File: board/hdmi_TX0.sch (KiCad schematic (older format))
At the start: 26 parts

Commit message: Updating from template.
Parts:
- removed CTX009: 0.33uF, Capacitors_SMD:C_0603, symbol C
- removed CTX010, CTX011: 0.1uF, Capacitors_SMD:C_0603, symbol C
- removed RTX006: 100K, Resistors_SMD:R_0402, symbol R
- removed UTX001: ΜA78L00, ma78l00:μA78L00, symbol ΜA78L00
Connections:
- net labels removed: VCC12V0
- wire segments 122 -> 125
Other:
- note added: "This sheet is generated from ../external/templates/\nDO NOT MODIFY!!!\n7e53b7f"
- note removed: "This sheet is generated from ../external/templates/\nDO NOT MODIFY!!!\nc4498e4"
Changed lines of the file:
@@
 LIBS:contrib
 LIBS:valves
-LIBS:pmod
+LIBS:pmod-conn_6x2
+LIBS:ma78l00
 LIBS:hdmi
 LIBS:ptn3363
-LIBS:ma78l00
-LIBS:pmod-conn_6x2
-LIBS:EEPROM
-LIBS:xc9140
-LIBS:hdmi-expansion-module-cache
+LIBS:hdmi_TXn-cache
 EELAYER 25 0
 EELAYER END
 $Descr A3 16535 11693
 encoding utf-8
-Sheet 2 2
+Sheet 1 1
 Title ""
 Date ""
@@
 F 0 "DTX001" H 10600 5540 50  0000 C CNN
 F 1 "D" H 10600 5340 50  0000 C CNN
-F 2 "Diodes_SMD:SOD-523" H 10600 5440 50  0000 C CNN
+F 2 "Diodes_SMD:SOD-523" H 10600 5440 50  0001 C CNN
 F 3 "" H 10600 5440 50  0000 C CNN
 F 4 "BAS16XV2T1G" H 10600 5440 60  0001 C CNN "manf#"
@@
 AR Path="/57C07751" Ref="RTX008"  Part="1"
 AR Path="/57C01383/57C07751" Ref="RTX003"  Part="1"
-AR Path="/5802F547/57C07751" Ref="RTX008"  Part="1"
 F 0 "RTX008" V 10700 4950 50  0000 C CNN
 F 1 "27K" V 10607 4951 50  0000 C CNN
@@
 AR Path="/57C07753" Ref="RTX002"  Part="1"
 AR Path="/57C01383/57C07753" Ref="RTX001"  Part="1"
-AR Path="/5802F547/57C07753" Ref="RTX002"  Part="1"
 F 0 "RTX002" V 3800 4400 50  0000 C CNN
 F 1 "2k2" V 3907 4401 50  0000 C CNN
@@
 AR Path="/57C07755" Ref="RTX001"  Part="1"
 AR Path="/57C01383/57C07755" Ref="RTX002"  Part="1"
-AR Path="/5802F547/57C07755" Ref="RTX001"  Part="1"
 F 0 "RTX001" V 4080 4400 50  0000 C CNN
 F 1 "2k2" V 4007 4401 50  0000 C CNN
@@
 	11750 4850 11600 4850
 Wire Wire Line
-	11600 4850 11600 6900
+	11600 4850 11600 5150
+Wire Wire Line
+	11600 5150 11600 5450
+Wire Wire Line
+	11600 5450 11600 5750
+Wire Wire Line
+	11600 5750 11600 6350
+Wire Wire Line
+	11600 6350 11600 6900
 Wire Wire Line
 	11750 5150 11600 5150
@@
 	6400 5800 6750 5800
 Wire Wire Line
-	8150 6600 9000 6600
+	8150 6600 8550 6600
+Wire Wire Line
+	8550 6600 9000 6600
 Wire Wire Line
 	8150 6400 9000 6400
 Wire Wire Line
-	7400 3750 7500 3750
-Wire Wire Line
-	7450 3750 7450 3600
+	7400 3750 7450 3750
+Wire Wire Line
+	7450 3750 7500 3750
+Wire Wire Line
+	7450 3200 7450 3750
 Connection ~ 7450 3750
 Wire Wire Line
@@
 Connection ~ 11600 6350
 Wire Wire Line
-	9800 5950 11750 5950
+	9800 5950 10600 5950
+Wire Wire Line
+	10600 5950 11750 5950
 Wire Wire Line
 	10600 5950 10600 5590
@@
 	4000 4100 4000 4250
 Wire Wire Line
-	3900 4100 4000 4100
+	3900 4100 3950 4100
+Wire Wire Line
+	3950 4100 4000 4100
 Text Label 3800 5900 2    60   ~ 0
 HDMIP_TX0_SCL
@@
 AR Path="/57C07769" Ref="RTX004"  Part="1"
 AR Path="/57C01383/57C07769" Ref="RTX004"  Part="1"
-AR Path="/5802F547/57C07769" Ref="RTX004"  Part="1"
 F 0 "RTX004" V 3800 5600 50  0000 C CNN
 F 1 "2k2" V 3907 5601 50  0000 C CNN
@@
 AR Path="/57B7FCE7" Ref="RTX005"  Part="1"
 AR Path="/57C01383/57B7FCE7" Ref="RTX005"  Part="1"
-AR Path="/5802F547/57B7FCE7" Ref="RTX005"  Part="1"
 F 0 "RTX005" V 4080 5600 50  0000 C CNN
 F 1 "2k2" V 4007 5601 50  0000 C CNN
@@
 AR Path="/57C0776D" Ref="RTX003"  Part="1"
 AR Path="/57C01383/57C0776D" Ref="RTX006"  Part="1"
-AR Path="/5802F547/57C0776D" Ref="RTX003"  Part="1"
 F 0 "RTX003" V 6580 6900 50  0000 C CNN
 F 1 "12k4" V 6507 6901 50  0000 C CNN
@@
 	3900 5300 3900 5450
 Wire Wire Line
-	3900 5300 4000 5300
+	3900 5300 3950 5300
+Wire Wire Line
+	3950 5300 4000 5300
 Wire Wire Line
 	4000 5300 4000 5450
@@
 AR Path="/57C07777" Ref="CTX017"  Part="1"
 AR Path="/57C01383/57C07777" Ref="CTX002"  Part="1"
-AR Path="/5802F547/57C07777" Ref="CTX017"  Part="1"
 F 0 "CTX017" H 8300 3750 30  0000 L CNN
 F 1 "100n" H 8300 3850 30  0000 L CNN
@@
 AR Path="/57C07779" Ref="CTX016"  Part="1"
 AR Path="/57C01383/57C07779" Ref="CTX001"  Part="1"
-AR Path="/5802F547/57C07779" Ref="CTX016"  Part="1"
 F 0 "CTX016" H 8350 3750 30  0000 L CNN
 F 1 "100n" H 8400 3850 30  0000 L CNN
@@
 $EndComp
 Wire Wire Line
-	8300 3600 8500 3600
+	8300 3600 8400 3600
+Wire Wire Line
+	8400 3600 8500 3600
 Wire Wire Line
 	8300 3600 8300 3700
@@
 	8300 4000 8300 4100
 Wire Wire Line
-	8300 4100 8500 4100
+	8300 4100 8400 4100
+Wire Wire Line
+	8400 4100 8500 4100
 Wire Wire Line
 	8500 4100 8500 4000
@@
 Text Label 9000 6400 2    60   ~ 0
 HDMI_TX0_HIZ_EN
-Text Label 1885 6870 0    60   ~ 0
+Text Label 4685 6670 2    60   ~ 0
 HDMI_TX0_HPD
+Text Label 4685 6570 2    60   ~ 0
+HDMI_TX0_SCL
 Text Label 1885 6670 0    60   ~ 0
-HDMI_TX0_SCL
-Text Label 1885 6770 0    60   ~ 0
 HDMI_TX0_SDA
 $Comp
@@
 	6500 7050 6500 7150
 Text Notes 670  10960 0    197  ~ 39
-This sheet is generated from ../external/templates/\nDO NOT MODIFY!!!\nc4498e4
-Wire Wire Line
-	2255 6970 2865 6970
-Wire Wire Line
-	2725 7070 2865 7070
+This sheet is generated from ../external/templates/\nDO NOT MODIFY!!!\n7e53b7f
+Wire Wire Line
+	2255 6970 2325 6970
+Wire Wire Line
+	2325 6970 2865 6970
+Wire Wire Line
+	2725 7070 2770 7070
+Wire Wire Line
+	2770 7070 2865 7070
 Wire Wire Line
 	2865 6570 1885 6570
@@
 	3755 6970 3665 6970
 Connection ~ 2325 6970
-Text Label 4685 6865 2    60   ~ 0
+Text Label 4685 6870 2    60   ~ 0
 HDMI_TX0_DDET
-Text Label 4685 6665 2    60   ~ 0
+Text Label 1885 6770 0    60   ~ 0
 HDMI_TX0_EQ1
-Text Label 4685 6765 2    60   ~ 0
+Text Label 1885 6870 0    60   ~ 0
 HDMI_TX0_DDC_EN
 Wire Wire Line
-	4685 6865 3665 6870
-Wire Wire Line
-	4685 6765 3665 6770
-Wire Wire Line
-	4685 6665 3665 6670
-Wire Wire Line
-	4685 6565 3665 6570
-Text Label 4685 6565 2    60   ~ 0
+	4685 6870 3665 6870
+Wire Wire Line
+	4685 6770 3665 6770
+Wire Wire Line
+	4685 6670 3665 6670
+Wire Wire Line
+	4685 6570 3665 6570
+Text Label 4685 6770 2    60   ~ 0
 HDMI_TX0_EQ0
 $Comp
@@
 	0    1    1    0
 $EndComp
-$Comp
-L ΜA78L00 UTX001
-U 1 1 57E8C5A1
-P 11700 8100
-F 0 "UTX001" H 12000 7800 60  0000 C CNN
-F 1 "ΜA78L00" H 11550 8350 60  0000 C CNN
-F 2 "ma78l00:μA78L00" H 11700 8100 60  0001 C CNN
-F 3 "" H 11700 8100 60  0000 C CNN
-F 4 "UA78L05ACPK" H 11700 8100 60  0001 C CNN "manf#"
-F 5 "296-11118-1-ND" H 11700 8100 60  0001 C CNN "digikey#"
-	1    11700 8100
-	1    0    0    -1
-$EndComp
-$Comp
-L C CTX009
-U 1 1 57E8C7B4
-P 10700 8400
-F 0 "CTX009" H 10725 8500 50  0000 L CNN
-F 1 "0.33uF" H 10725 8300 50  0000 L CNN
-F 2 "Capacitors_SMD:C_0603" H 10738 8250 50  0001 C CNN
-F 3 "" H 10700 8400 50  0000 C CNN
-	1    10700 8400
-	1    0    0    -1
-$EndComp
-$Comp
-L C CTX010
-U 1 1 57E8C84C
-P 12450 8400
-F 0 "CTX010" H 12475 8500 50  0000 L CNN
-F 1 "0.1uF" H 12475 8300 50  0000 L CNN
-F 2 "Capacitors_SMD:C_0603" H 12488 8250 50  0001 C CNN
-F 3 "" H 12450 8400 50  0000 C CNN
-	1    12450 8400
-	1    0    0    -1
-$EndComp
-$Comp
-L C CTX011
-U 1 1 57E8C9BD
-P 12800 8400
-F 0 "CTX011" H 12825 8500 50  0000 L CNN
-F 1 "0.1uF" H 12825 8300 50  0000 L CNN
-F 2 "Capacitors_SMD:C_0603" H 12838 8250 50  0001 C CNN
-F 3 "" H 12800 8400 50  0000 C CNN
-	1    12800 8400
-	1    0    0    -1
-$EndComp
-$Comp
-L R RTX006
-U 1 1 57E8CA09
-P 13100 8400
-F 0 "RTX006" V 13180 8400 50  0000 C CNN
-F 1 "100K" V 13100 8400 50  0000 C CNN
-F 2 "Resistors_SMD:R_0402" V 13030 8400 50  0001 C CNN
-F 3 "" H 13100 8400 50  0000 C CNN
-	1    13100 8400
-	1    0    0    -1
-$EndComp
-Wire Wire Line
-	10700 8250 10700 8100
-Wire Wire Line
-	10350 8100 11050 8100
-Wire Wire Line
-	12350 8100 13850 8100
-Wire Wire Line
-	12450 8100 12450 8250
-Wire Wire Line
-	12800 8100 12800 8250
-Connection ~ 12450 8100
-Wire Wire Line
-	13100 8100 13100 8250
-Connection ~ 12800 8100
-Wire Wire Line
-	10700 8550 10700 8700
-Wire Wire Line
-	10700 8700 13100 8700
-Wire Wire Line
-	11700 8650 11700 8750
-Wire Wire Line
-	12450 8700 12450 8550
-Connection ~ 11700 8700
-Wire Wire Line
-	12800 8700 12800 8550
-Connection ~ 12450 8700
-Wire Wire Line
-	13100 8700 13100 8550
-Connection ~ 12800 8700
-Text Label 10700 8100 0    60   ~ 0
-VCC12V0
-Connection ~ 10700 8100
-Text GLabel 10350 8100 0    60   Input ~ 0
-VCC12V0
-Connection ~ 13100 8100
-Text Label 13850 8100 2    60   ~ 0
-TX05V0
-$Comp
-L GND #PWR113
-U 1 1 57E8D9CD
-P 11700 8750
-F 0 "#PWR113" H 11700 8500 60  0001 C CNN
-F 1 "GND" H 11700 8600 60  0000 C CNN
-F 2 "" H 11700 8750 60  0000 C CNN
-F 3 "" H 11700 8750 60  0000 C CNN
-	1    11700 8750
-	1    0    0    -1
-$EndComp
-Text Label 11700 8700 0    60   ~ 0
-GND
-Text GLabel 10300 7650 0    60   Input ~ 0
+Text GLabel 7025 3200 0    60   Input ~ 0
 VCC3V3
-Wire Wire Line
-	10300 7650 10650 7650
 $Comp
 L PMOD-CONN_6X2 PTX0
@@
 	1    0    0    -1
 $EndComp
-Text Label 7450 3600 0    60   ~ 0
-VCC3V3
-Wire Wire Line
-	8400 3600 8400 3515
-Text Label 8400 3515 0    60   ~ 0
-VCC3V3
 Text Label 10600 4450 0    60   ~ 0
 VCC3V3
-Text Label 10650 7650 2    60   ~ 0
+Text Label 8400 3200 2    60   ~ 0
 VCC3V3
 Text Label 3950 4050 0    60   ~ 0
@@
 Text Label 2725 7070 2    60   ~ 0
 VCC3V3
+Text Label 7575 2975 2    60   ~ 0
+TX05V0
+Text GLabel 7025 2975 0    60   Input ~ 0
+TX05V0
+Wire Wire Line
+	7025 3200 7450 3200
+Wire Wire Line
+	7450 3200 8400 3200
+Wire Wire Line
+	8400 3200 8400 3600
+Connection ~ 7450 3200
+Wire Wire Line
+	7025 2975 7575 2975
 $EndSCHEMATC

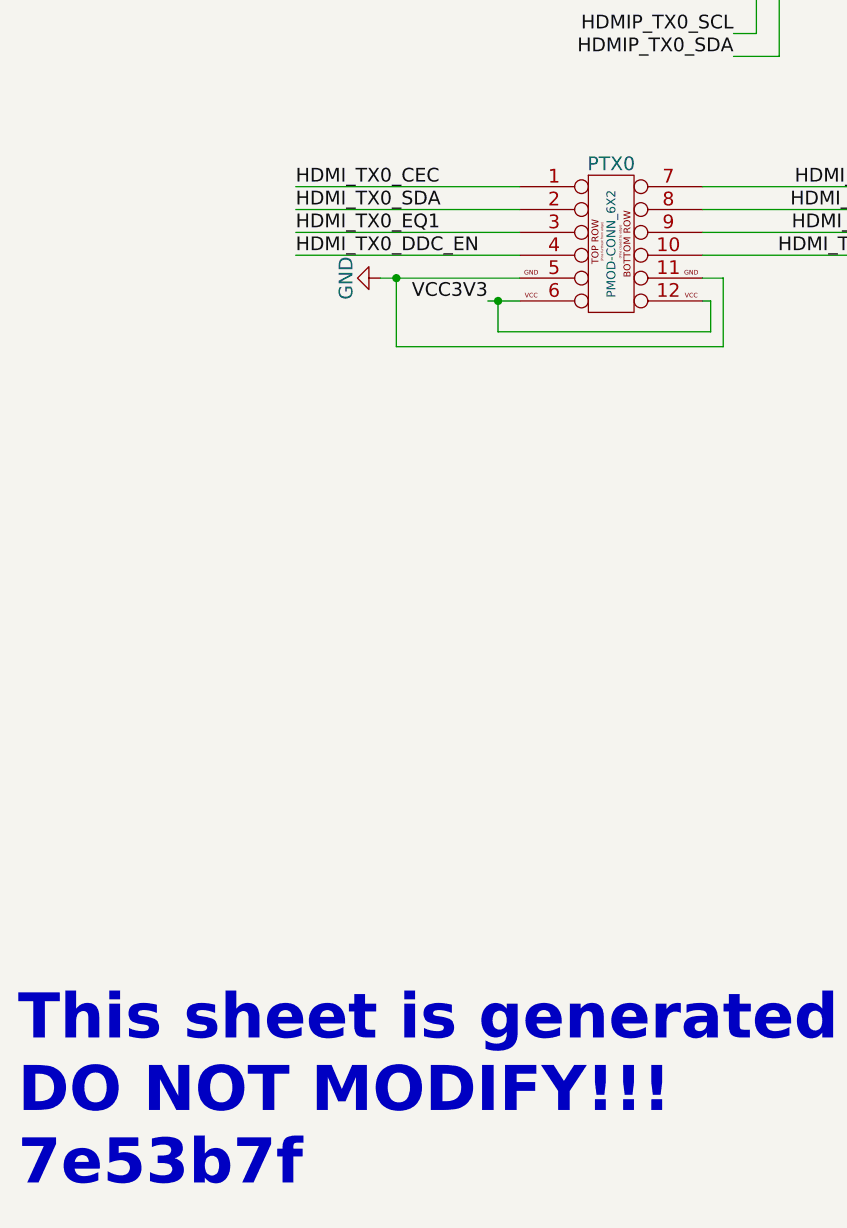
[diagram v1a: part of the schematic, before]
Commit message: Update from template.
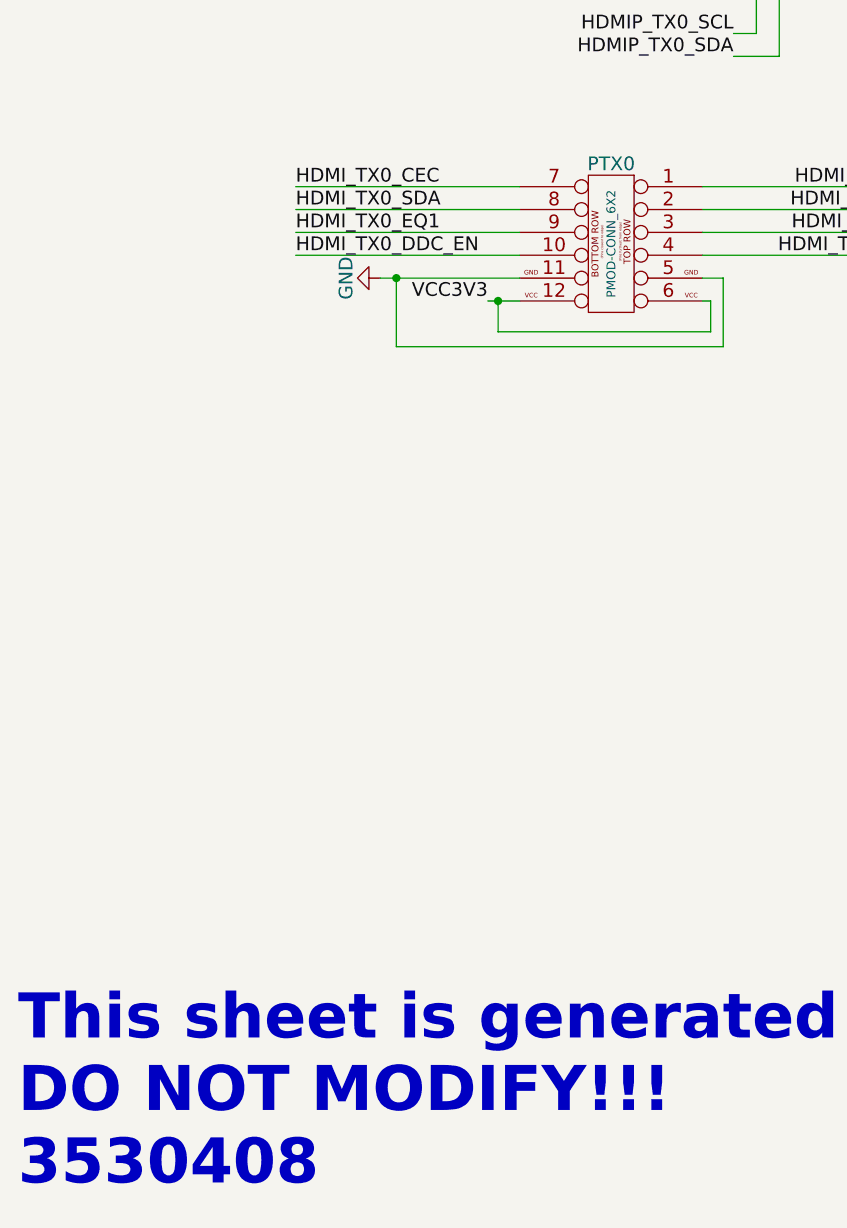
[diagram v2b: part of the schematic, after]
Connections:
- net HDMI_TX0_CEC: now also PTX0.7 (P7); no longer PTX0.1 (P1)
- net HDMI_TX0_DDC_EN: now also PTX0.10 (P10); no longer PTX0.4 (P4)
- net HDMI_TX0_DDET: now also PTX0.4 (P4); no longer PTX0.10 (P10)
- net HDMI_TX0_EQ0: now also PTX0.3 (P3); no longer PTX0.9 (P9)
- net HDMI_TX0_EQ1: now also PTX0.9 (P9); no longer PTX0.3 (P3)
- net HDMI_TX0_HPD: now also PTX0.2 (P2); no longer PTX0.8 (P8)
- net HDMI_TX0_SCL: now also PTX0.1 (P1); no longer PTX0.7 (P7)
- net HDMI_TX0_SDA: now also PTX0.8 (P8); no longer PTX0.2 (P2)
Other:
- note added: "This sheet is generated from ../external/templates/\nDO NOT MODIFY!!!\n3530408"
- note removed: "This sheet is generated from ../external/templates/\nDO NOT MODIFY!!!\n7e53b7f"
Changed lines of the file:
@@
 LIBS:hdmi
 LIBS:ptn3363
-LIBS:hdmi_TXn-cache
 EELAYER 25 0
 EELAYER END
@@
 	6500 7050 6500 7150
 Text Notes 670  10960 0    197  ~ 39
-This sheet is generated from ../external/templates/\nDO NOT MODIFY!!!\n7e53b7f
+This sheet is generated from ../external/templates/\nDO NOT MODIFY!!!\n3530408
 Wire Wire Line
 	2255 6970 2325 6970
@@
 F 3 "" H 3265 6820 60  0000 C CNN
 	1    3265 6820
-	1    0    0    -1
+	-1   0    0    -1
 $EndComp
 Text Label 10600 4450 0    60   ~ 0

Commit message: Update from tempaltes.
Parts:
- PTX0: footprint (none) -> pmod:pmod_pin_array_6x2
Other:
- note added: "This sheet is generated from ../external/templates/\nDO NOT MODIFY!!!\nee70a4a"
- note removed: "This sheet is generated from ../external/templates/\nDO NOT MODIFY!!!\n3530408"
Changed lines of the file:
@@
 HDMIP_TX0_HPD
 $Comp
-L GND #PWR106
+L GND #PWR01
 U 1 1 57B7C214
 P 7450 7150
-F 0 "#PWR106" H 7450 6900 60  0001 C CNN
+F 0 "#PWR01" H 7450 6900 60  0001 C CNN
 F 1 "GND" H 7450 7000 60  0000 C CNN
 F 2 "" H 7450 7150 60  0000 C CNN
@@
 $EndComp
 $Comp
-L GND #PWR112
+L GND #PWR02
 U 1 1 57C0774B
 P 11600 6900
-F 0 "#PWR112" H 11600 6650 60  0001 C CNN
+F 0 "#PWR02" H 11600 6650 60  0001 C CNN
 F 1 "GND" H 11600 6750 60  0000 C CNN
 F 2 "" H 11600 6900 60  0000 C CNN
@@
 	11750 4850 11600 4850
 Wire Wire Line
-	11600 4850 11600 5150
-Wire Wire Line
-	11600 5150 11600 5450
-Wire Wire Line
-	11600 5450 11600 5750
-Wire Wire Line
-	11600 5750 11600 6350
-Wire Wire Line
-	11600 6350 11600 6900
+	11600 4850 11600 6900
 Wire Wire Line
 	11750 5150 11600 5150
@@
 	6400 5800 6750 5800
 Wire Wire Line
-	8150 6600 8550 6600
-Wire Wire Line
-	8550 6600 9000 6600
+	8150 6600 9000 6600
 Wire Wire Line
 	8150 6400 9000 6400
 Wire Wire Line
-	7400 3750 7450 3750
-Wire Wire Line
-	7450 3750 7500 3750
+	7400 3750 7500 3750
 Wire Wire Line
 	7450 3200 7450 3750
@@
 Connection ~ 11600 6350
 Wire Wire Line
-	9800 5950 10600 5950
-Wire Wire Line
-	10600 5950 11750 5950
+	9800 5950 11750 5950
 Wire Wire Line
 	10600 5950 10600 5590
@@
 	4000 4100 4000 4250
 Wire Wire Line
-	3900 4100 3950 4100
-Wire Wire Line
-	3950 4100 4000 4100
+	3900 4100 4000 4100
 Text Label 3800 5900 2    60   ~ 0
 HDMIP_TX0_SCL
@@
 	6500 6300 6500 6750
 $Comp
-L GND #PWR104
+L GND #PWR03
 U 1 1 57C0776F
 P 6500 7150
-F 0 "#PWR104" H 6500 6900 60  0001 C CNN
+F 0 "#PWR03" H 6500 6900 60  0001 C CNN
 F 1 "GND" H 6500 7000 60  0000 C CNN
 F 2 "" H 6500 7150 60  0000 C CNN
@@
 	3900 5300 3900 5450
 Wire Wire Line
-	3900 5300 3950 5300
-Wire Wire Line
-	3950 5300 4000 5300
+	3900 5300 4000 5300
 Wire Wire Line
 	4000 5300 4000 5450
@@
 $EndComp
 $Comp
-L GND #PWR109
+L GND #PWR04
 U 1 1 57C07776
 P 8550 7150
-F 0 "#PWR109" H 8550 6900 60  0001 C CNN
+F 0 "#PWR04" H 8550 6900 60  0001 C CNN
 F 1 "GND" H 8550 7000 60  0000 C CNN
 F 2 "" H 8550 7150 60  0000 C CNN
@@
 $EndComp
 Wire Wire Line
-	8300 3600 8400 3600
-Wire Wire Line
-	8400 3600 8500 3600
+	8300 3600 8500 3600
 Wire Wire Line
 	8300 3600 8300 3700
@@
 	8300 4000 8300 4100
 Wire Wire Line
-	8300 4100 8400 4100
-Wire Wire Line
-	8400 4100 8500 4100
+	8300 4100 8500 4100
 Wire Wire Line
 	8500 4100 8500 4000
 $Comp
-L GND #PWR108
+L GND #PWR05
 U 1 1 57C0777E
 P 8400 4150
-F 0 "#PWR108" H 8400 3900 60  0001 C CNN
+F 0 "#PWR05" H 8400 3900 60  0001 C CNN
 F 1 "GND" H 8400 4000 60  0000 C CNN
 F 2 "" H 8400 4150 60  0000 C CNN
@@
 HDMI_TX0_SDA
 $Comp
-L GND #PWR101
+L GND #PWR06
 U 1 1 57C07784
 P 2255 6970
-F 0 "#PWR101" H 2255 6720 60  0001 C CNN
+F 0 "#PWR06" H 2255 6720 60  0001 C CNN
 F 1 "GND" H 2255 6820 60  0000 C CNN
 F 2 "" H 2255 6970 60  0000 C CNN
@@
 	6500 7050 6500 7150
 Text Notes 670  10960 0    197  ~ 39
-This sheet is generated from ../external/templates/\nDO NOT MODIFY!!!\n3530408
-Wire Wire Line
-	2255 6970 2325 6970
-Wire Wire Line
-	2325 6970 2865 6970
-Wire Wire Line
-	2725 7070 2770 7070
-Wire Wire Line
-	2770 7070 2865 7070
+This sheet is generated from ../external/templates/\nDO NOT MODIFY!!!\nee70a4a
+Wire Wire Line
+	2255 6970 2865 6970
+Wire Wire Line
+	2725 7070 2865 7070
 Wire Wire Line
 	2865 6570 1885 6570
@@
 F 0 "PTX0" H 3265 7170 60  0000 C CNN
 F 1 "PMOD-CONN_6X2" V 3265 6820 39  0000 C CNN
-F 2 "" H 3265 6820 60  0000 C CNN
+F 2 "pmod:pmod_pin_array_6x2" H 3265 6820 60  0001 C CNN
 F 3 "" H 3265 6820 60  0000 C CNN
 	1    3265 6820
@@
 TX05V0
 Wire Wire Line
-	7025 3200 7450 3200
-Wire Wire Line
-	7450 3200 8400 3200
+	7025 3200 8400 3200
 Wire Wire Line
 	8400 3200 8400 3600
